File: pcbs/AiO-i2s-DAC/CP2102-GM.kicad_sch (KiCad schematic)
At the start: 12 parts, among them U4 CP2102-GM

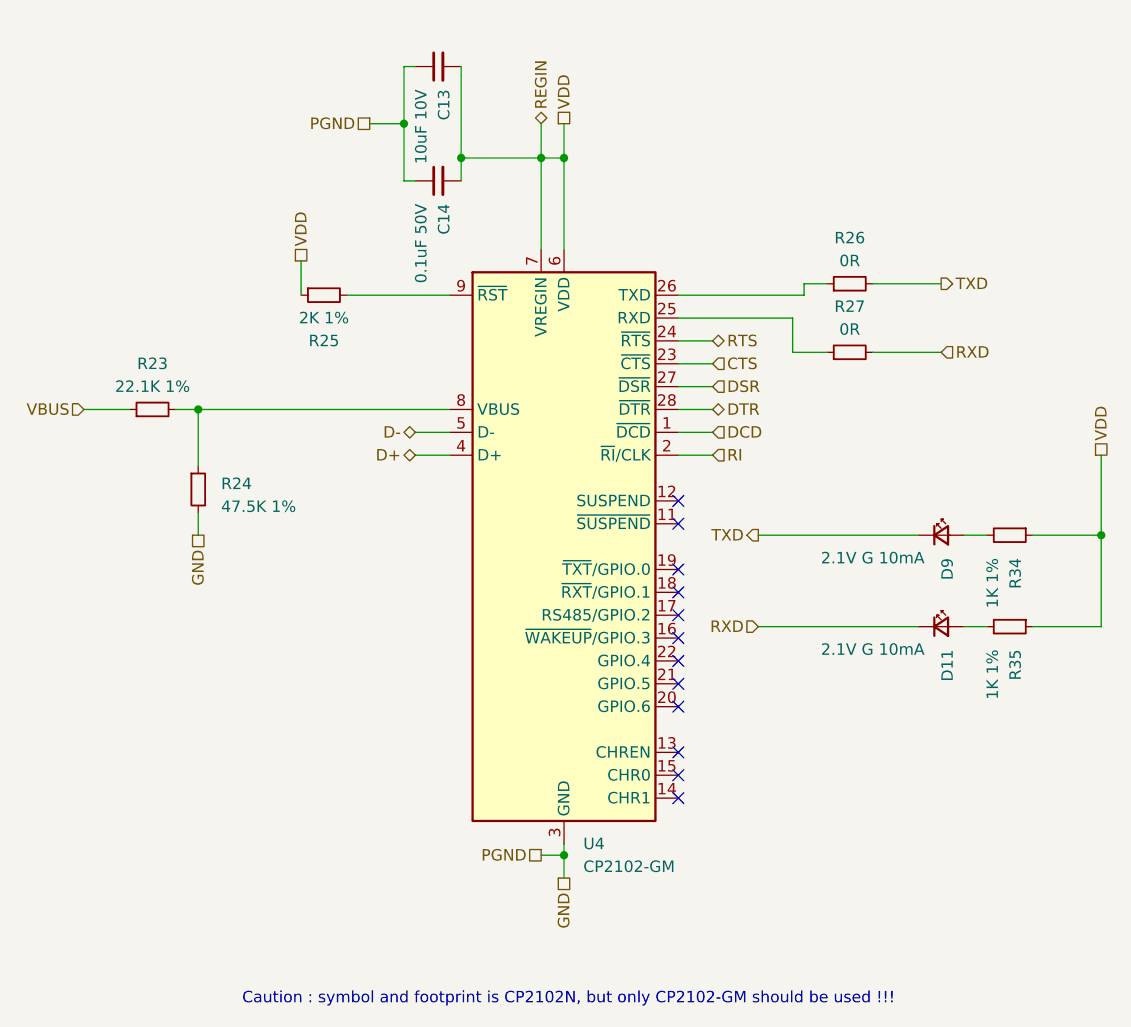
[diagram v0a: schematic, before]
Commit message: Adding equivalent JLCPCB values
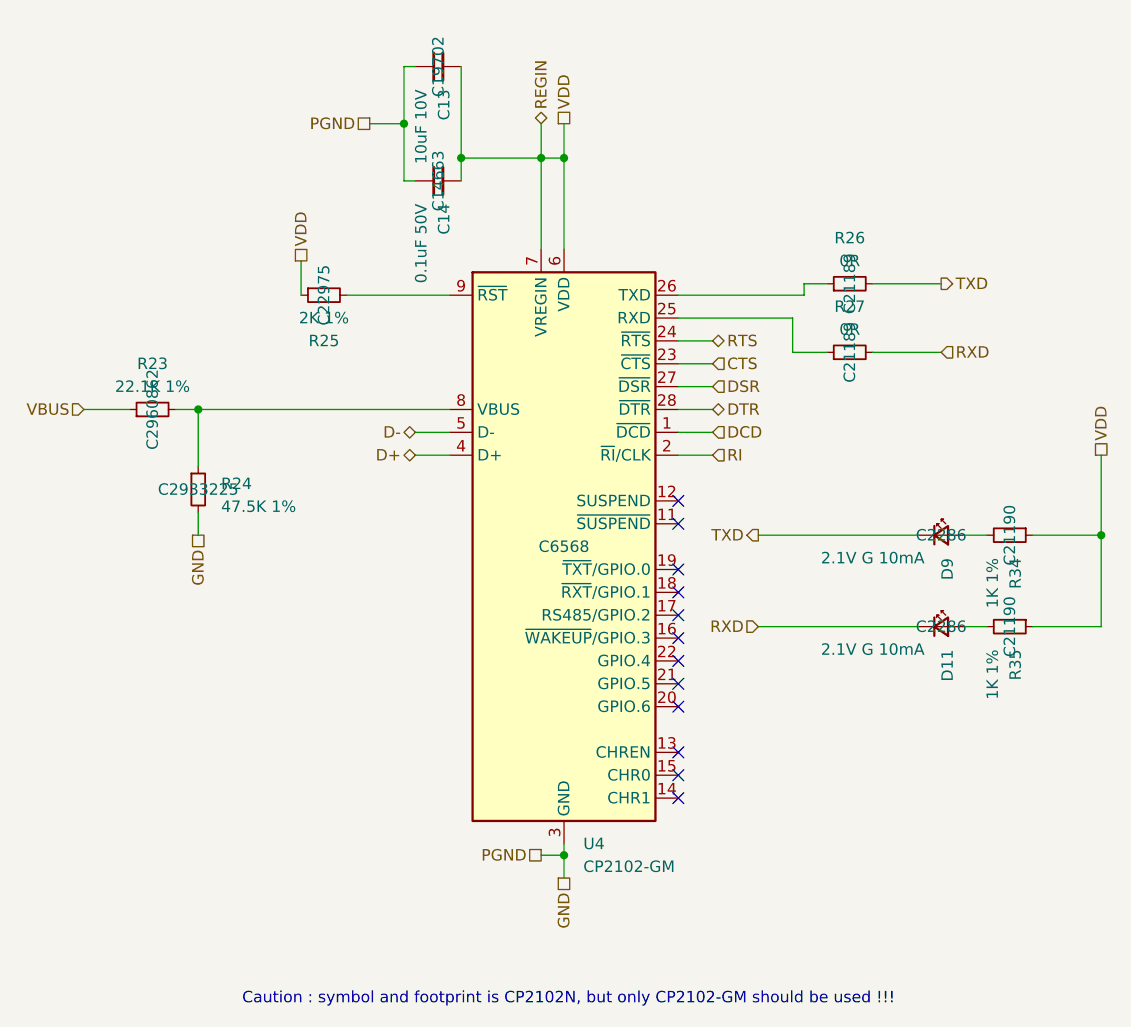
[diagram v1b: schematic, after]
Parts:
- C13: LCSC (none) -> C19702
- C14: LCSC (none) -> C14663
- D11, D9: LCSC (none) -> C2286
- R23: LCSC (none) -> C2960862
- R24: LCSC (none) -> C2933225
- R25: LCSC (none) -> C22975
- R26, R27: LCSC (none) -> C21189
- R34, R35: LCSC (none) -> C21190
- U4: LCSC (none) -> C6568
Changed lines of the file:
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@@
+			)
+		)
+		(property "LCSC" "C21190"
+			(at 203.2 100.33 0)
+			(effects
+				(font
+					(size 1.27 1.27)
+				)
 			)
 		)
@@
 			)
 		)
+		(property "LCSC" "C14663"
+			(at 139.7 60.96 0)
+			(effects
+				(font
+					(size 1.27 1.27)
+				)
+			)
+		)
 		(pin "1"
 		)
@@
 			)
 		)
+		(property "LCSC" "C2286"
+			(at 195.58 110.49 0)
+			(effects
+				(font
+					(size 1.27 1.27)
+				)
+			)
+		)
 		(pin "1"
 		)
@@
 				)
 				(hide yes)
+			)
+		)
+		(property "LCSC" "C2286"
+			(at 195.58 100.33 0)
+			(effects
+				(font
+					(size 1.27 1.27)
+				)
 			)
 		)
@@
 			)
 		)
+		(property "LCSC" "C21189"
+			(at 185.42 80.01 0)
+			(effects
+				(font
+					(size 1.27 1.27)
+				)
+			)
+		)
 		(pin "1"
 		)
@@
 			)
 		)
+		(property "LCSC" "C19702"
+			(at 139.7 48.26 0)
+			(effects
+				(font
+					(size 1.27 1.27)
+				)
+			)
+		)
 		(pin "1"
 		)
@@
 			)
 		)
+		(property "LCSC" "C2960862"
+			(at 107.95 86.36 0)
+			(effects
+				(font
+					(size 1.27 1.27)
+				)
+			)
+		)
 		(pin "1"
 		)
@@
 			)
 		)
+		(property "LCSC" "C21190"
+			(at 203.2 110.49 0)
+			(effects
+				(font
+					(size 1.27 1.27)
+				)
+			)
+		)
 		(pin "1"
 		)
@@
 			)
 		)
+		(property "LCSC" "C21189"
+			(at 185.42 72.39 0)
+			(effects
+				(font
+					(size 1.27 1.27)
+				)
+			)
+		)
 		(pin "1"
 		)
@@
 			)
 		)
+		(property "LCSC" "C22975"
+			(at 127 73.66 0)
+			(effects
+				(font
+					(size 1.27 1.27)
+				)
+			)
+		)
 		(pin "1"
 		)
@@
 			)
 		)
+		(property "LCSC" "C2933225"
+			(at 113.03 95.25 0)
+			(effects
+				(font
+					(size 1.27 1.27)
+				)
+			)
+		)
 		(pin "1"
 		)
@@
 			)
 		)
+		(property "LCSC" "C6568"
+			(at 153.67 101.6 0)
+			(effects
+				(font
+					(size 1.27 1.27)
+				)
+			)
+		)

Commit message: LCSC BOM Preparation
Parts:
- C13: LCSC alt (none) -> C6119842
- C14: LCSC alt (none) -> C1591
- D11, D9: LCSC alt (none) -> C125093
- R23: LCSC alt (none) -> C2960862
- R24: LCSC alt (none) -> C2933225
- R25: LCSC alt (none) -> C237750
- R26, R27: LCSC alt (none) -> C21189
- R34, R35: LCSC alt (none) -> C22548
- U4: LCSC alt (none) -> C6568
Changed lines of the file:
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@@
+			)
+		)
+		(property "LCSC alt" "C22548"
+			(at 203.2 100.33 0)
+			(effects
+				(font
+					(size 1.27 1.27)
+				)
 			)
 		)
@@
 			)
 		)
+		(property "LCSC alt" "C1591"
+			(at 139.7 60.96 0)
+			(effects
+				(font
+					(size 1.27 1.27)
+				)
+			)
+		)
 		(pin "1"
 		)
@@
 			)
 		)
+		(property "LCSC alt" "C125093"
+			(at 195.58 110.49 0)
+			(effects
+				(font
+					(size 1.27 1.27)
+				)
+			)
+		)
 		(pin "1"
 		)
@@
 		)
 		(property "LCSC" "C2286"
+			(at 195.58 100.33 0)
+			(effects
+				(font
+					(size 1.27 1.27)
+				)
+			)
+		)
+		(property "LCSC alt" "C125093"
 			(at 195.58 100.33 0)
 			(effects
@@
 			)
 		)
+		(property "LCSC alt" "C21189"
+			(at 185.42 80.01 0)
+			(effects
+				(font
+					(size 1.27 1.27)
+				)
+			)
+		)
 		(pin "1"
 		)
@@
 			)
 		)
+		(property "LCSC alt" "C6119842"
+			(at 139.7 48.26 0)
+			(effects
+				(font
+					(size 1.27 1.27)
+				)
+			)
+		)
 		(pin "1"
 		)
@@
 			)
 		)
+		(property "LCSC alt" "C2960862"
+			(at 107.95 86.36 0)
+			(effects
+				(font
+					(size 1.27 1.27)
+				)
+			)
+		)
 		(pin "1"
 		)
@@
 			)
 		)
+		(property "LCSC alt" "C22548"
+			(at 203.2 110.49 0)
+			(effects
+				(font
+					(size 1.27 1.27)
+				)
+			)
+		)
 		(pin "1"
 		)
@@
 			)
 		)
+		(property "LCSC alt" "C21189"
+			(at 185.42 72.39 0)
+			(effects
+				(font
+					(size 1.27 1.27)
+				)
+			)
+		)
 		(pin "1"
 		)
@@
 			)
 		)
+		(property "LCSC alt" "C237750"
+			(at 127 73.66 0)
+			(effects
+				(font
+					(size 1.27 1.27)
+				)
+			)
+		)
 		(pin "1"
 		)
@@
 			)
 		)
+		(property "LCSC alt" "C2933225"
+			(at 113.03 95.25 0)
+			(effects
+				(font
+					(size 1.27 1.27)
+				)
+			)
+		)
 		(pin "1"
 		)
@@
 			(at 153.67 101.6 0)
 			(effects
+				(font
+					(size 1.27 1.27)
+				)
+			)
+		)
+		(property "LCSC alt" "C6568"
+			(at 153.67 101.6 0)
+			(effects

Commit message: Build prep
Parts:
- R23: LCSC C2960862 -> C6397988
- R24: LCSC C2933225 -> C403243
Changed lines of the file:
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@@
 					(size 1.27 1.27)
 				)
+				(hide yes)
 			)
 		)
@@
 					(size 1.27 1.27)
 				)
+				(hide yes)
 			)
 		)
@@
 					(size 1.27 1.27)
 				)
+				(hide yes)
 			)
 		)
@@
 					(size 1.27 1.27)
 				)
+				(hide yes)
 			)
 		)
@@
 					(size 1.27 1.27)
 				)
+				(hide yes)
 			)
 		)
@@
 					(size 1.27 1.27)
 				)
+				(hide yes)
 			)
 		)
@@
 					(size 1.27 1.27)
 				)
+				(hide yes)
 			)
 		)
@@
 					(size 1.27 1.27)
 				)
+				(hide yes)
 			)
 		)
@@
 					(size 1.27 1.27)
 				)
+				(hide yes)
 			)
 		)
@@
 					(size 1.27 1.27)
 				)
+				(hide yes)
 			)
 		)
@@
 					(size 1.27 1.27)
 				)
+				(hide yes)
 			)
 		)
@@
 					(size 1.27 1.27)
 				)
+				(hide yes)
 			)
 		)
@@
 			)
 		)
-		(property "LCSC" "C2960862"
+		(property "LCSC" "C6397988"
 			(at 107.95 86.36 0)
 			(effects
@@
 					(size 1.27 1.27)
 				)
+				(hide yes)
 			)
 		)
@@
 					(size 1.27 1.27)
 				)
+				(hide yes)
 			)
 		)
@@
 					(size 1.27 1.27)
 				)
+				(hide yes)
 			)
 		)
@@
 					(size 1.27 1.27)
 				)
+				(hide yes)
 			)
 		)
@@
 					(size 1.27 1.27)
 				)
+				(hide yes)
 			)
 		)
@@
 					(size 1.27 1.27)
 				)
+				(hide yes)
 			)
 		)
@@
 					(size 1.27 1.27)
 				)
+				(hide yes)
 			)
 		)
@@
 					(size 1.27 1.27)
 				)
+				(hide yes)
 			)
 		)
@@
 			)
 		)
-		(property "LCSC" "C2933225"
+		(property "LCSC" "C403243"
 			(at 113.03 95.25 0)
 			(effects
@@
 					(size 1.27 1.27)
 				)
+				(hide yes)
 			)
 		)
@@
 					(size 1.27 1.27)
 				)
+				(hide yes)
 			)
 		)
@@
 					(size 1.27 1.27)
 				)
+				(hide yes)
 			)
 		)
@@
 					(size 1.27 1.27)
 				)
-			)
-		)
+				(hide yes)
+			)
+		)
